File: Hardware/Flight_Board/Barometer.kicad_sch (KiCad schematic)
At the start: 3 parts

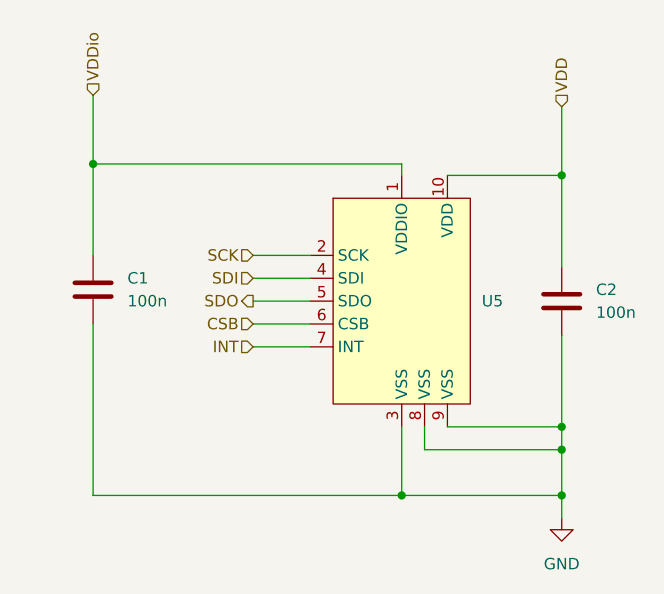
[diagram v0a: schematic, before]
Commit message: standardize connections and create initial spi2 bus
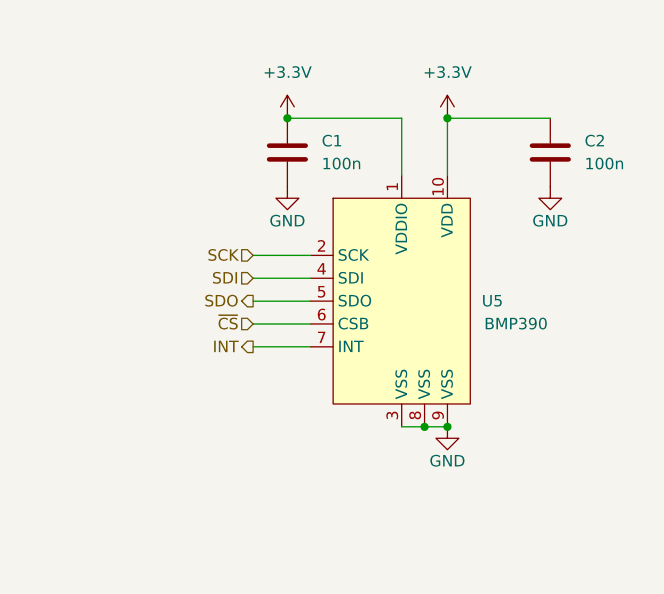
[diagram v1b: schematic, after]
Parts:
- U5: value ~ -> BMP390
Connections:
- net VDDio is gone; now on net +3.3V: C1.1, U5.1 (VDDIO)
- net CSB renamed ~{CS}
- net VDD renamed +3.3V
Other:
- moved on the sheet: C1, C2

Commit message: clean up and finalize initial design
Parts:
- renumbered C1 to C15, C2 to C16, U5 to U4
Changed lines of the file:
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@@
   (symbol (lib_id "Device:C") (at 160.02 76.2 0) (unit 1)
     (in_bom yes) (on_board yes) (dnp no) (fields_autoplaced)
-    (property "Reference" "C1" (at 163.83 74.93 0)
+    (property "Reference" "C15" (at 163.83 74.93 0)
       (effects (font (size 1.27 1.27)) (justify left))
     )
@@
       (project "Flight_Board"
         (path "/e8eb85d5-f1ff-4500-895d-25b9ff5f6d36/438715e3-b069-4320-9581-dc19d9c2cf0e"
-          (reference "C1") (unit 1)
+          (reference "C15") (unit 1)
         )
       )
@@
   (symbol (lib_id "power:+3.3V") (at 177.8 72.39 0) (unit 1)
     (in_bom yes) (on_board yes) (dnp no) (fields_autoplaced)
-    (property "Reference" "#PWR023" (at 177.8 76.2 0)
+    (property "Reference" "#PWR028" (at 177.8 76.2 0)
       (effects (font (size 1.27 1.27)) hide)
     )
@@
       (project "Flight_Board"
         (path "/e8eb85d5-f1ff-4500-895d-25b9ff5f6d36/438715e3-b069-4320-9581-dc19d9c2cf0e"
-          (reference "#PWR023") (unit 1)
+          (reference "#PWR028") (unit 1)
         )
       )
@@
   (symbol (lib_id "Device:C") (at 189.23 76.2 0) (unit 1)
     (in_bom yes) (on_board yes) (dnp no) (fields_autoplaced)
-    (property "Reference" "C2" (at 193.04 74.93 0)
+    (property "Reference" "C16" (at 193.04 74.93 0)
       (effects (font (size 1.27 1.27)) (justify left))
     )
@@
       (project "Flight_Board"
         (path "/e8eb85d5-f1ff-4500-895d-25b9ff5f6d36/438715e3-b069-4320-9581-dc19d9c2cf0e"
-          (reference "C2") (unit 1)
+          (reference "C16") (unit 1)
         )
       )
@@
   (symbol (lib_id "power:+3.3V") (at 160.02 72.39 0) (unit 1)
     (in_bom yes) (on_board yes) (dnp no) (fields_autoplaced)
-    (property "Reference" "#PWR025" (at 160.02 76.2 0)
+    (property "Reference" "#PWR026" (at 160.02 76.2 0)
       (effects (font (size 1.27 1.27)) hide)
     )
@@
       (project "Flight_Board"
         (path "/e8eb85d5-f1ff-4500-895d-25b9ff5f6d36/438715e3-b069-4320-9581-dc19d9c2cf0e"
-          (reference "#PWR025") (unit 1)
+          (reference "#PWR026") (unit 1)
         )
       )
@@
   (symbol (lib_id "power:GND") (at 189.23 80.01 0) (unit 1)
     (in_bom yes) (on_board yes) (dnp no)
-    (property "Reference" "#PWR022" (at 189.23 86.36 0)
+    (property "Reference" "#PWR030" (at 189.23 86.36 0)
       (effects (font (size 1.27 1.27)) hide)
     )
@@
       (project "Flight_Board"
         (path "/e8eb85d5-f1ff-4500-895d-25b9ff5f6d36/438715e3-b069-4320-9581-dc19d9c2cf0e"
-          (reference "#PWR022") (unit 1)
+          (reference "#PWR030") (unit 1)
         )
       )
@@
   (symbol (lib_id "Project:BMP390") (at 175.26 92.71 0) (unit 1)
     (in_bom yes) (on_board yes) (dnp no)
-    (property "Reference" "U5" (at 181.61 92.71 0)
+    (property "Reference" "U4" (at 181.61 92.71 0)
       (effects (font (size 1.27 1.27)) (justify left))
     )
@@
       (project "Flight_Board"
         (path "/e8eb85d5-f1ff-4500-895d-25b9ff5f6d36/438715e3-b069-4320-9581-dc19d9c2cf0e"
-          (reference "U5") (unit 1)
+          (reference "U4") (unit 1)
         )
       )
@@
   (symbol (lib_id "power:GND") (at 177.8 106.68 0) (unit 1)
     (in_bom yes) (on_board yes) (dnp no)
-    (property "Reference" "#PWR016" (at 177.8 113.03 0)
+    (property "Reference" "#PWR029" (at 177.8 113.03 0)
       (effects (font (size 1.27 1.27)) hide)
     )
@@
       (project "Flight_Board"
         (path "/e8eb85d5-f1ff-4500-895d-25b9ff5f6d36/438715e3-b069-4320-9581-dc19d9c2cf0e"
-          (reference "#PWR016") (unit 1)
+          (reference "#PWR029") (unit 1)
         )
       )
@@
   (symbol (lib_id "power:GND") (at 160.02 80.01 0) (unit 1)
     (in_bom yes) (on_board yes) (dnp no)
-    (property "Reference" "#PWR024" (at 160.02 86.36 0)
+    (property "Reference" "#PWR027" (at 160.02 86.36 0)
       (effects (font (size 1.27 1.27)) hide)
     )
@@
       (project "Flight_Board"
         (path "/e8eb85d5-f1ff-4500-895d-25b9ff5f6d36/438715e3-b069-4320-9581-dc19d9c2cf0e"
-          (reference "#PWR024") (unit 1)
+          (reference "#PWR027") (unit 1)
         )
       )

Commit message: Add LEDs and test points
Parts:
- added TP2: BARO_INT, symbol Connector:TestPoint
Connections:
- net INT: now also TP2.1
- net SDI renamed MOSI
- net SDO renamed MISO
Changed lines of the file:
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@@
   (junction (at 160.02 72.39) (diameter 0) (color 0 0 0 0)
   )
+  (junction (at 139.7 97.79) (diameter 0) (color 0 0 0 0)
+  )
   (wire (pts (xy 177.8 78.74) (xy 177.8 72.39))
     (stroke (width 0) (type default))
@@
     (stroke (width 0) (type default))
   )
+  (wire (pts (xy 139.7 93.98) (xy 139.7 97.79))
+    (stroke (width 0) (type default))
+  )
   (wire (pts (xy 172.72 72.39) (xy 172.72 78.74))
     (stroke (width 0) (type default))
   )
-  (wire (pts (xy 156.21 97.79) (xy 162.56 97.79))
+  (wire (pts (xy 135.89 97.79) (xy 139.7 97.79))
     (stroke (width 0) (type default))
   )
@@
     (stroke (width 0) (type default))
   )
+  (wire (pts (xy 139.7 97.79) (xy 162.56 97.79))
+    (stroke (width 0) (type default))
+  )
   (wire (pts (xy 172.72 106.68) (xy 175.26 106.68))
     (stroke (width 0) (type default))
@@
     (effects (font (size 1.27 1.27)) (justify right))
   )
-  (hierarchical_label "SDI" (shape input) (at 156.21 90.17 180) (fields_autoplaced)
+  (hierarchical_label "MOSI" (shape input) (at 156.21 90.17 180) (fields_autoplaced)
     (effects (font (size 1.27 1.27)) (justify right))
   )
@@
     (effects (font (size 1.27 1.27)) (justify right))
   )
-  (hierarchical_label "INT" (shape output) (at 156.21 97.79 180) (fields_autoplaced)
-    (effects (font (size 1.27 1.27)) (justify right))
-  )
-  (hierarchical_label "SDO" (shape output) (at 156.21 92.71 180) (fields_autoplaced)
+  (hierarchical_label "INT" (shape output) (at 135.89 97.79 180) (fields_autoplaced)
+    (effects (font (size 1.27 1.27)) (justify right))
+  )
+  (hierarchical_label "MISO" (shape output) (at 156.21 92.71 180) (fields_autoplaced)
     (effects (font (size 1.27 1.27)) (justify right))
   )
@@
         )
       )
+    )
+  )
+  (symbol (lib_id "Connector:TestPoint") (at 139.7 93.98 0) (unit 1)
+    (in_bom yes) (on_board yes) (dnp no)
+    (property "Reference" "TP2" (at 144.78 90.678 90)
+      (effects (font (size 1.27 1.27)) hide)
+    )
+    (property "Value" "BARO_INT" (at 138.43 88.9 0)
+      (effects (font (size 1.27 1.27)) (justify left))
+    )
+    (property "Footprint" "" (at 144.78 93.98 0)
+      (effects (font (size 1.27 1.27)) hide)
+    )
+    (property "Datasheet" "~" (at 144.78 93.98 0)
+      (effects (font (size 1.27 1.27)) hide)
+    )
+    (pin "1")
+    (instances
+      (project "Flight_Board"
+        (path "/e8eb85d5-f1ff-4500-895d-25b9ff5f6d36/bc23ea56-d50e-4ce7-856f-e38dfbe72971"
+          (reference "TP2") (unit 1)
+        )
+        (path "/e8eb85d5-f1ff-4500-895d-25b9ff5f6d36/43c0adf1-436b-4b66-9010-44cf9a79cc96"
+          (reference "TP3") (unit 1)
+        )
+        (path "/e8eb85d5-f1ff-4500-895d-25b9ff5f6d36/7c06db2a-34f5-45c0-9668-fbbbd940678c"
+          (reference "TP11") (unit 1)
+        )
+        (path "/e8eb85d5-f1ff-4500-895d-25b9ff5f6d36/52cae81a-54fe-42c0-9a19-be88b271d004"
+          (reference "TP14") (unit 1)
+        )
+        (path "/e8eb85d5-f1ff-4500-895d-25b9ff5f6d36/676308d2-6f42-4cc0-804f-a459182d1a62"
+          (reference "TP16") (unit 1)
+        )
+        (path "/e8eb85d5-f1ff-4500-895d-25b9ff5f6d36/438715e3-b069-4320-9581-dc19d9c2cf0e"
+          (reference "TP17") (unit 1)
+        )
+      )

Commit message: final touches, bom, footprints
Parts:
- C15, C16: footprint (none) -> Capacitor_SMD:C_0603_1608Metric_Pad1.08x0.95mm_HandSolder
- TP2: footprint (none) -> TestPoint:TestPoint_THTPad_2.0x2.0mm_Drill1.0mm
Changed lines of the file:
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@@
       (effects (font (size 1.27 1.27)) (justify left))
     )
-    (property "Footprint" "" (at 160.9852 80.01 0)
+    (property "Footprint" "Capacitor_SMD:C_0603_1608Metric_Pad1.08x0.95mm_HandSolder" (at 160.9852 80.01 0)
       (effects (font (size 1.27 1.27)) hide)
     )
@@
       (effects (font (size 1.27 1.27)) (justify left))
     )
-    (property "Footprint" "" (at 190.1952 80.01 0)
+    (property "Footprint" "Capacitor_SMD:C_0603_1608Metric_Pad1.08x0.95mm_HandSolder" (at 190.1952 80.01 0)
       (effects (font (size 1.27 1.27)) hide)
     )
@@
       (effects (font (size 1.27 1.27)) (justify left))
     )
-    (property "Footprint" "" (at 144.78 93.98 0)
-      (effects (font (size 1.27 1.27)) hide)
-    )
+    (property "Footprint" "TestPoint:TestPoint_THTPad_2.0x2.0mm_Drill1.0mm" (at 144.78 93.98 0)
+      (effects (font (size 1.27 1.27)) hide)
+    )

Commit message: minor tweaks and prettification
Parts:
- TP2: footprint TestPoint:TestPoint_THTPad_2.0x2.0mm_Drill1.0mm -> TestPoint:TestPoint_Pad_D1.0mm
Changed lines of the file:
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@@
       (effects (font (size 1.27 1.27)) (justify left))
     )
-    (property "Footprint" "TestPoint:TestPoint_THTPad_2.0x2.0mm_Drill1.0mm" (at 144.78 93.98 0)
+    (property "Footprint" "TestPoint:TestPoint_Pad_D1.0mm" (at 144.78 93.98 0)
       (effects (font (size 1.27 1.27)) hide)
     )
